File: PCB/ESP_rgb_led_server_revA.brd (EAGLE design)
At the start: 68.3 x 51.3 mm, 33 parts, among them U1 AMS1117, U2 ESP-12F

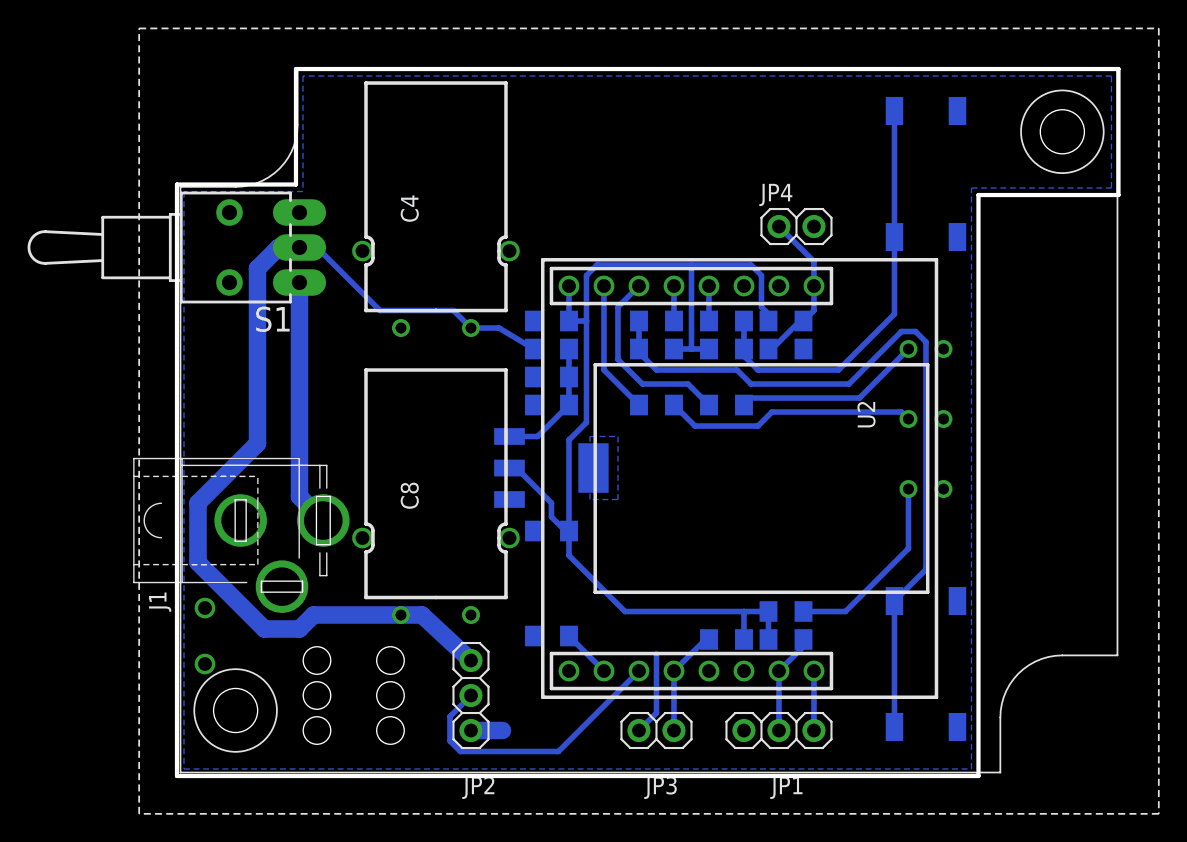
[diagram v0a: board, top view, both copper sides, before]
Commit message: added: schematics and layout exported as images
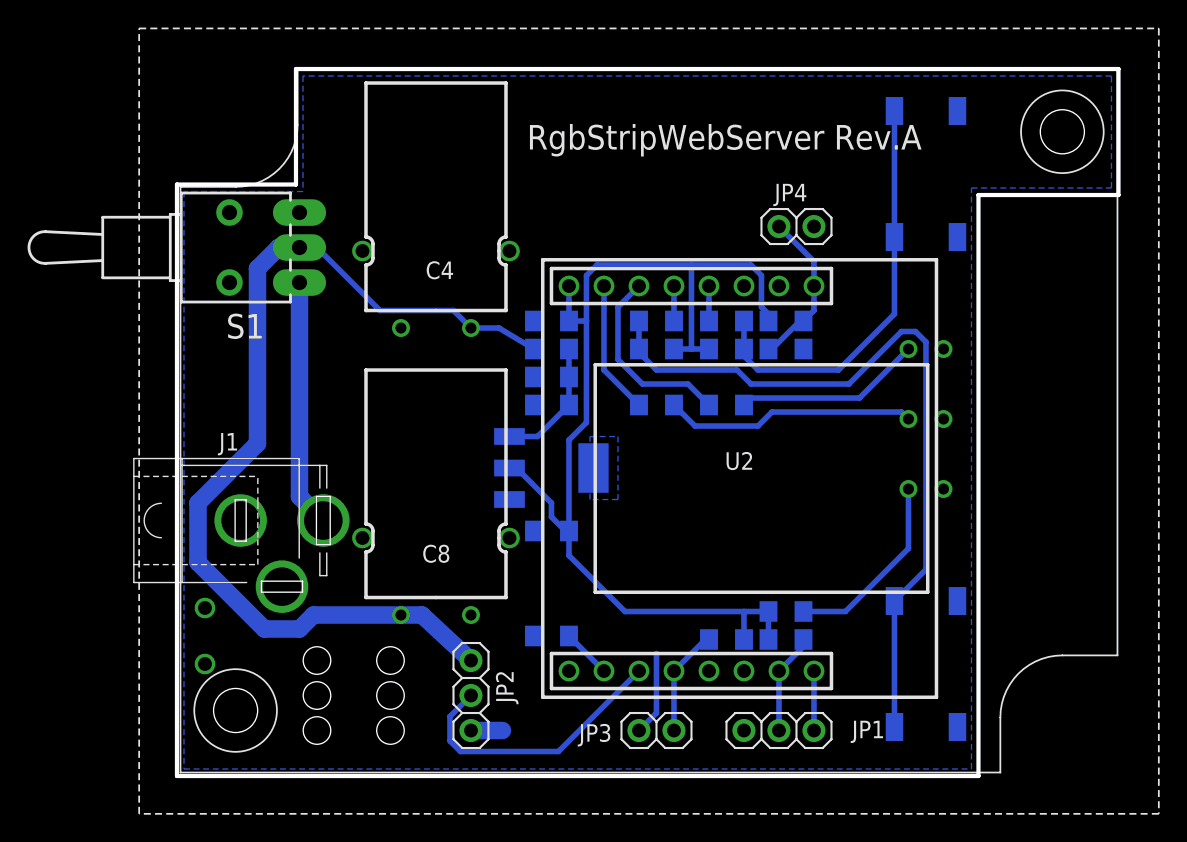
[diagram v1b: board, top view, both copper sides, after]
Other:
- board text added: "RgbStripWebServer Rev.A"
